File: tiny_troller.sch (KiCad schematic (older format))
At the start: 30 parts, among them U1 MA702GQ-P, U3 STM32G071G8U6, U5 MCP2025-330E_MD, U6 MAX14870ETC+T

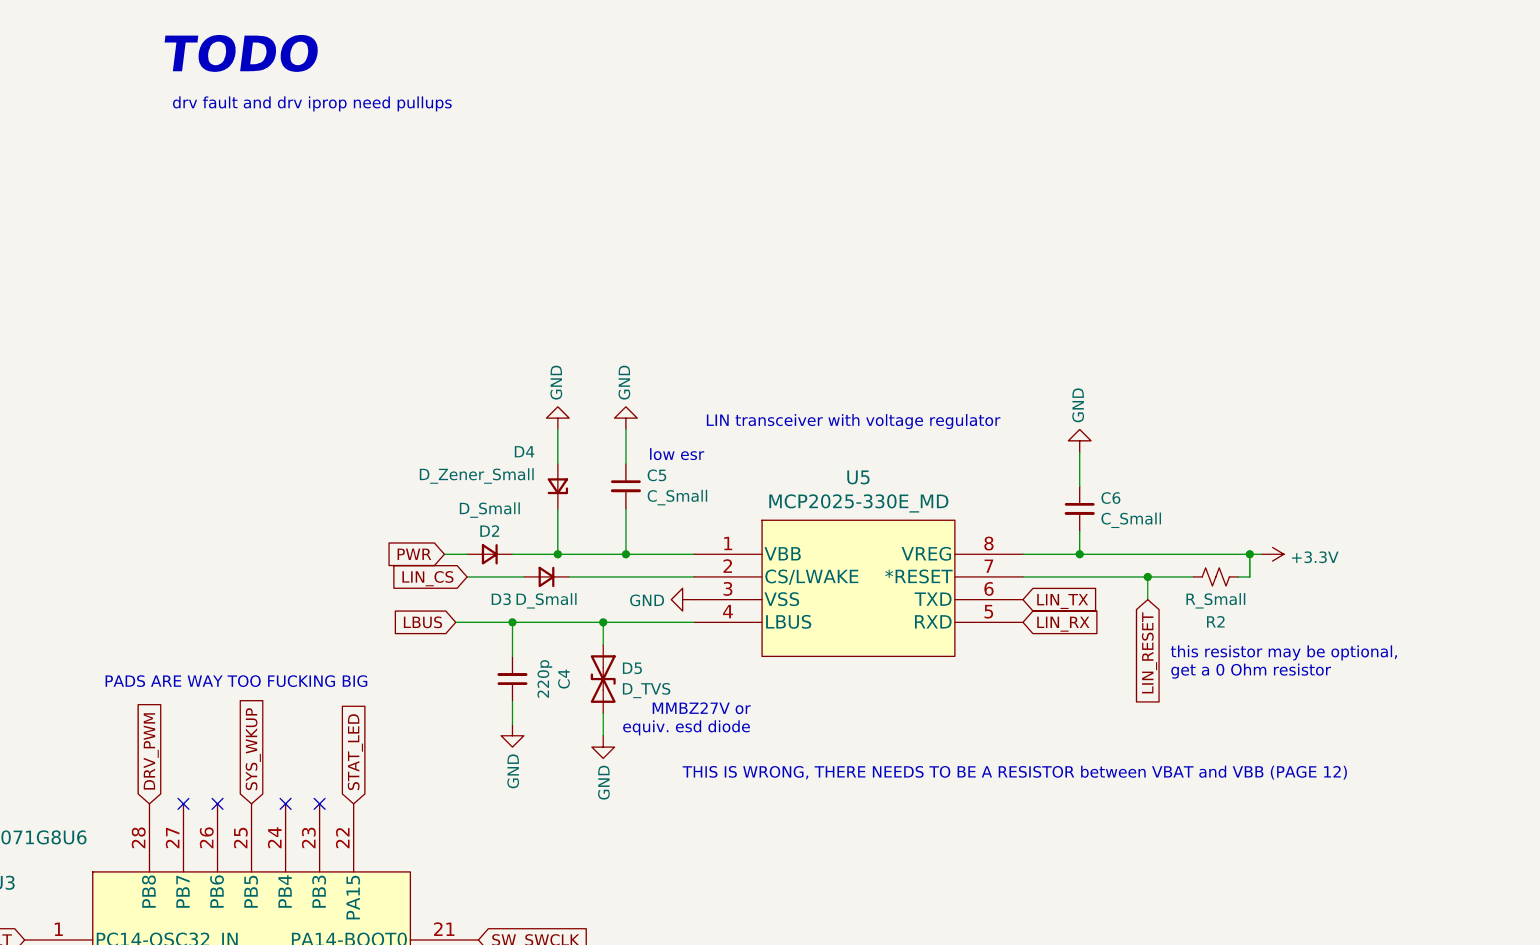
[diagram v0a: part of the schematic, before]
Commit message: R5 added, circuitry for MCP2025 LIN transceiver and regulator VBB pin should be correct now.
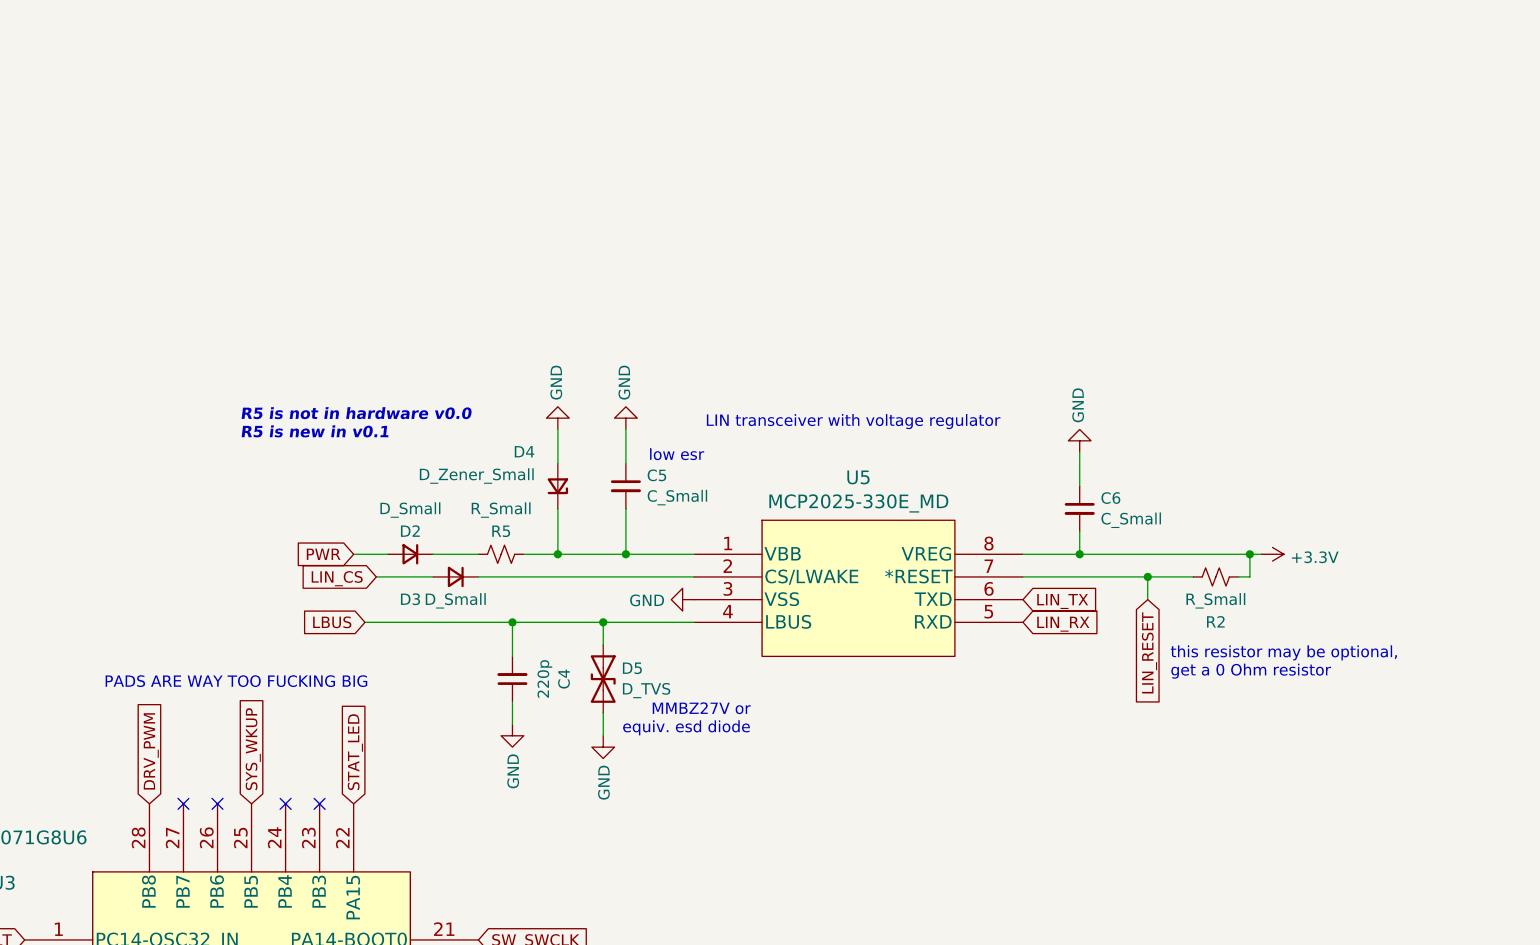
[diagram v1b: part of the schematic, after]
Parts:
- added R5: R_Small, Resistor_SMD:R_0402_1005Metric, symbol Device:R_Small_US
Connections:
- net at C5.2, D4.1 (K), U5.1 (VBB): now also R5.1; no longer D2.1 (K)
- new net: D2.1 (K), R5.2
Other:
- note added: "R5 is not in hardware v0.0\nR5 is new in v0.1"
- note removed: "THIS IS WRONG, THERE NEEDS TO BE A RESISTOR between VBAT and VBB (PAGE 12)"
- note removed: "TODO"
- note removed: "drv fault and drv iprop need pullups"
- moved on the sheet: D2, D3
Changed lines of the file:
@@
 Text GLabel 2800 7300 2    50   Input ~ 0
 STAT_LED
-Text Notes 5950 -550 0    157  Italic 31
-TODO
 Text GLabel 1850 1850 0    50   Input ~ 0
 LBUS
@@
 	0    1    1    0
 $EndComp
-Text Notes 6000 -400 0    50   ~ 0
-drv fault and drv iprop need pullups
 Text GLabel 7350 4000 2    50   Input ~ 0
 ENC_MGH
@@
 Wire Wire Line
 	10000 1250 10000 1100
-Text GLabel 7250 1850 0    50   Input ~ 0
+Text GLabel 6850 1850 0    50   Input ~ 0
 LBUS
 $Comp
@@
 L Device:D_Small D2
 U 1 1 615AA4A8
-P 7400 1550
-F 0 "D2" H 7400 1450 50  0000 C CNN
-F 1 "D_Small" H 7400 1350 50  0000 C CNN
-F 2 "Diode_SMD:D_0402_1005Metric" V 7400 1550 50  0001 C CNN
-F 3 "~" V 7400 1550 50  0001 C CNN
-	1    7400 1550
+P 7050 1550
+F 0 "D2" H 7050 1450 50  0000 C CNN
+F 1 "D_Small" H 7050 1350 50  0000 C CNN
+F 2 "Diode_SMD:D_0402_1005Metric" V 7050 1550 50  0001 C CNN
+F 3 "~" V 7050 1550 50  0001 C CNN
+	1    7050 1550
 	-1   0    0    1
 $EndComp
-Text GLabel 7200 1550 0    50   Input ~ 0
+Text GLabel 6800 1550 0    50   Input ~ 0
 PWR
 Wire Wire Line
@@
 Wire Wire Line
 	8000 1150 8000 1000
-Wire Wire Line
-	7500 1550 7700 1550
-Connection ~ 7700 1550
 $Comp
 L Device:C_Small C4
@@
 $EndComp
 Wire Wire Line
-	7250 1850 7500 1850
+	6850 1850 7500 1850
 Wire Wire Line
 	7500 1850 7500 2000
@@
 L Device:D_Small D3
 U 1 1 61617327
-P 7650 1650
-F 0 "D3" H 7850 1750 50  0000 C CNN
-F 1 "D_Small" H 7650 1750 50  0000 C CNN
-F 2 "Diode_SMD:D_0402_1005Metric" V 7650 1650 50  0001 C CNN
-F 3 "~" V 7650 1650 50  0001 C CNN
-	1    7650 1650
+P 7250 1650
+F 0 "D3" H 7450 1750 50  0000 C CNN
+F 1 "D_Small" H 7250 1750 50  0000 C CNN
+F 2 "Diode_SMD:D_0402_1005Metric" V 7250 1650 50  0001 C CNN
+F 3 "~" V 7250 1650 50  0001 C CNN
+	1    7250 1650
 	-1   0    0    1
 $EndComp
-Text GLabel 7300 1650 0    50   Input ~ 0
+Text GLabel 6900 1650 0    50   Input ~ 0
 LIN_CS
 Wire Wire Line
-	7300 1650 7550 1650
-Wire Wire Line
-	7750 1650 8300 1650
+	6900 1650 7150 1650
+Wire Wire Line
+	7350 1650 8300 1650
 $Comp
 L Device:C_Small C6
@@
 $EndComp
 Wire Wire Line
-	7200 1550 7300 1550
+	6800 1550 6950 1550
 Text Notes 5700 2150 0    50   ~ 0
 PADS ARE WAY TOO FUCKING BIG
@@
 	0    1    1    0
 $EndComp
-Text Notes 8250 2550 0    50   ~ 0
-THIS IS WRONG, THERE NEEDS TO BE A RESISTOR between VBAT and VBB (PAGE 12)
 Text Notes 10400 2100 0    50   ~ 0
 this resistor may be optional,\nget a 0 Ohm resistor
+$Comp
+L Device:R_Small_US R5
+U 1 1 618DD948
+P 7450 1550
+F 0 "R5" V 7350 1550 50  0000 C CNN
+F 1 "R_Small" V 7250 1550 50  0000 C CNN
+F 2 "Resistor_SMD:R_0402_1005Metric" H 7450 1550 50  0001 C CNN
+F 3 "~" H 7450 1550 50  0001 C CNN
+	1    7450 1550
+	0    1    1    0
+$EndComp
+Wire Wire Line
+	7550 1550 7700 1550
+Connection ~ 7700 1550
+Wire Wire Line
+	7350 1550 7150 1550
+Text Notes 6300 1050 0    50   Italic 10
+R5 is not in hardware v0.0\nR5 is new in v0.1
 $EndSCHEMATC

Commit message: v01 design first pass done (all components selected for the first time).
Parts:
- added C3: 100n, Capacitor_SMD:C_0402_1005Metric, symbol Device:C_Small
- C5: value C_Small -> 22u; V_max (none) -> 6.3V
- C6: value C_Small -> 10u; V_max (none) -> 6.3V
- D2, D3: value D_Small -> CLS10F40,L3F
- D4: value D_Zener_Small -> CPDQC24VEU-HF
- D5: value D_TVS -> CPDQR24V-HF
- R2: value R_Small -> 10k
- R3: value R_Small_US -> 70m
- R4: value R_Small_US -> 10k
- R5: value R_Small -> 2
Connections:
- net GND: now also C3.1
- net at D3.1 (K), U5.2 (CS/LWAKE): now also C3.2
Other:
- note added: "R2 and D3 may be optional,\ntry with 0 Ohm resistor instead"
- note removed: "MMBZ27V or\nequiv. esd diode"
- note removed: "PADS ARE WAY TOO FUCKING BIG"
- note removed: "low esr"
- note removed: "this resistor may be optional,\nget a 0 Ohm resistor"
- moved on the sheet: C4, C5, D3, D4, D5
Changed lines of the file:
@@
 Wire Wire Line
 	10000 1250 10000 1100
-Text GLabel 6850 1850 0    50   Input ~ 0
+Text GLabel 7600 1850 0    50   Input ~ 0
 LBUS
 $Comp
@@
 L Device:D_Zener_Small D4
 U 1 1 615A0B9A
-P 7700 1250
-F 0 "D4" V 7850 1150 50  0000 R CNN
-F 1 "D_Zener_Small" V 7750 1150 50  0000 R CNN
-F 2 "Diode_SMD:D_0402_1005Metric" V 7700 1250 50  0001 C CNN
-F 3 "~" V 7700 1250 50  0001 C CNN
-	1    7700 1250
+P 7700 1150
+F 0 "D4" V 7750 1050 50  0000 R CNN
+F 1 "CPDQC24VEU-HF" V 7650 1050 50  0000 R CNN
+F 2 "Diode_SMD:D_0402_1005Metric" V 7700 1150 50  0001 C CNN
+F 3 "~" V 7700 1150 50  0001 C CNN
+	1    7700 1150
 	0    1    -1   0
 $EndComp
@@
 U 1 1 615AA4A8
 P 7050 1550
-F 0 "D2" H 7050 1450 50  0000 C CNN
-F 1 "D_Small" H 7050 1350 50  0000 C CNN
+F 0 "D2" H 7050 1350 50  0000 C CNN
+F 1 "CLS10F40,L3F" H 7100 1450 50  0000 C CNN
 F 2 "Diode_SMD:D_0402_1005Metric" V 7050 1550 50  0001 C CNN
-F 3 "~" V 7050 1550 50  0001 C CNN
+F 3 "https://media.digikey.com/pdf/Data%20Sheets/Comchip%20PDFs/CPDQC24VEU-HF.pdf" V 7050 1550 50  0001 C CNN
 	1    7050 1550
 	-1   0    0    1
@@
 PWR
 Wire Wire Line
-	7700 1350 7700 1550
+	7700 1250 7700 1550
 Wire Wire Line
 	7700 1550 8000 1550
 Wire Wire Line
-	8000 1350 8000 1550
+	8000 1250 8000 1550
 Connection ~ 8000 1550
 Wire Wire Line
@@
 $EndComp
 Wire Wire Line
-	7700 1150 7700 1000
-Wire Wire Line
-	8000 1150 8000 1000
+	7700 1050 7700 1000
+Wire Wire Line
+	8000 1050 8000 1000
 $Comp
 L Device:C_Small C4
 U 1 1 615C8E0F
-P 7500 2100
-F 0 "C4" V 7271 2100 50  0000 C CNN
-F 1 "220p" V 7362 2100 50  0000 C CNN
-F 2 "Capacitor_SMD:C_0402_1005Metric" H 7500 2100 50  0001 C CNN
-F 3 "~" H 7500 2100 50  0001 C CNN
-	1    7500 2100
-	-1   0    0    1
-$EndComp
-Wire Wire Line
-	6850 1850 7500 1850
-Wire Wire Line
-	7500 1850 7500 2000
-Connection ~ 7500 1850
-Wire Wire Line
-	7500 1850 7900 1850
-Wire Wire Line
-	7900 1850 7900 1950
-Connection ~ 7900 1850
-Wire Wire Line
-	7900 1850 8300 1850
+P 7700 2100
+F 0 "C4" H 7850 2050 50  0000 C CNN
+F 1 "220p" H 7900 2150 50  0000 C CNN
+F 2 "Capacitor_SMD:C_0402_1005Metric" H 7700 2100 50  0001 C CNN
+F 3 "~" H 7700 2100 50  0001 C CNN
+	1    7700 2100
+	-1   0    0    1
+$EndComp
+Wire Wire Line
+	7700 1850 7700 2000
+Wire Wire Line
+	8000 1850 8000 1950
 $Comp
 L power:GND #PWR0108
 U 1 1 615DCA56
-P 7500 2300
-F 0 "#PWR0108" H 7500 2050 50  0001 C CNN
-F 1 "GND" V 7505 2172 50  0000 R CNN
-F 2 "" H 7500 2300 50  0001 C CNN
-F 3 "" H 7500 2300 50  0001 C CNN
-	1    7500 2300
+P 7700 2300
+F 0 "#PWR0108" H 7700 2050 50  0001 C CNN
+F 1 "GND" V 7705 2172 50  0000 R CNN
+F 2 "" H 7700 2300 50  0001 C CNN
+F 3 "" H 7700 2300 50  0001 C CNN
+	1    7700 2300
 	1    0    0    -1
 $EndComp
@@
 L power:GND #PWR0109
 U 1 1 615DD075
-P 7900 2350
-F 0 "#PWR0109" H 7900 2100 50  0001 C CNN
-F 1 "GND" V 7905 2222 50  0000 R CNN
-F 2 "" H 7900 2350 50  0001 C CNN
-F 3 "" H 7900 2350 50  0001 C CNN
-	1    7900 2350
-	1    0    0    -1
-$EndComp
-Wire Wire Line
-	7500 2200 7500 2300
-Wire Wire Line
-	7900 2250 7900 2350
-Text Notes 8550 2350 2    50   ~ 0
-MMBZ27V or\nequiv. esd diode
-Text Notes 8100 1150 0    50   ~ 0
-low esr
+P 8000 2350
+F 0 "#PWR0109" H 8000 2100 50  0001 C CNN
+F 1 "GND" V 8005 2222 50  0000 R CNN
+F 2 "" H 8000 2350 50  0001 C CNN
+F 3 "" H 8000 2350 50  0001 C CNN
+	1    8000 2350
+	1    0    0    -1
+$EndComp
+Wire Wire Line
+	7700 2200 7700 2300
+Wire Wire Line
+	8000 2250 8000 2350
 $Comp
 L Device:R_Small_US R2
@@
 P 10600 1650
 F 0 "R2" V 10400 1650 50  0000 C CNN
-F 1 "R_Small" V 10500 1650 50  0000 C CNN
+F 1 "10k" V 10500 1650 50  0000 C CNN
 F 2 "Resistor_SMD:R_0402_1005Metric" H 10600 1650 50  0001 C CNN
 F 3 "~" H 10600 1650 50  0001 C CNN
@@
 $EndComp
 Wire Wire Line
-	9750 1650 10300 1650
-Text GLabel 10300 1750 3    50   Input ~ 0
+	9750 1650 10250 1650
+Text GLabel 10250 1750 3    50   Input ~ 0
 LIN_RESET
 Wire Wire Line
-	10300 1750 10300 1650
-Connection ~ 10300 1650
-Wire Wire Line
-	10300 1650 10500 1650
+	10250 1750 10250 1650
 Connection ~ 10000 1550
 Wire Wire Line
@@
 L Device:D_Small D3
 U 1 1 61617327
-P 7250 1650
-F 0 "D3" H 7450 1750 50  0000 C CNN
-F 1 "D_Small" H 7250 1750 50  0000 C CNN
-F 2 "Diode_SMD:D_0402_1005Metric" V 7250 1650 50  0001 C CNN
-F 3 "~" V 7250 1650 50  0001 C CNN
-	1    7250 1650
-	-1   0    0    1
-$EndComp
-Text GLabel 6900 1650 0    50   Input ~ 0
+P 6800 1650
+F 0 "D3" H 6800 1750 50  0000 C CNN
+F 1 "CLS10F40,L3F" H 6800 1850 50  0000 C CNN
+F 2 "Diode_SMD:D_0402_1005Metric" V 6800 1650 50  0001 C CNN
+F 3 "~" V 6800 1650 50  0001 C CNN
+	1    6800 1650
+	-1   0    0    1
+$EndComp
+Text GLabel 6550 1650 0    50   Input ~ 0
 LIN_CS
 Wire Wire Line
-	6900 1650 7150 1650
-Wire Wire Line
-	7350 1650 8300 1650
+	6550 1650 6700 1650
+Wire Wire Line
+	6900 1650 7100 1650
 $Comp
 L Device:C_Small C6
 U 1 1 61637AA0
 P 10000 1350
-F 0 "C6" H 10092 1396 50  0000 L CNN
-F 1 "C_Small" H 10092 1305 50  0000 L CNN
+F 0 "C6" H 10100 1450 50  0000 L CNN
+F 1 "10u" H 10100 1350 50  0000 L CNN
 F 2 "Capacitor_SMD:C_0402_1005Metric" H 10000 1350 50  0001 C CNN
-F 3 "~" H 10000 1350 50  0001 C CNN
+F 3 "GRJ155R60J106ME11D" H 10000 1350 50  0001 C CNN
+F 4 "6.3V" H 10100 1300 50  0000 L TNN "V_max"
 	1    10000 1350
 	1    0    0    -1
@@
 L Device:C_Small C5
 U 1 1 61638882
-P 8000 1250
-F 0 "C5" H 8092 1296 50  0000 L CNN
-F 1 "C_Small" H 8092 1205 50  0000 L CNN
-F 2 "Capacitor_SMD:C_0402_1005Metric" H 8000 1250 50  0001 C CNN
-F 3 "~" H 8000 1250 50  0001 C CNN
-	1    8000 1250
+P 8000 1150
+F 0 "C5" H 8092 1196 50  0000 L CNN
+F 1 "22u" H 8092 1105 50  0000 L CNN
+F 2 "Capacitor_SMD:C_0402_1005Metric" H 8000 1150 50  0001 C CNN
+F 3 "04026D226MAT2A" H 8000 1150 50  0001 C CNN
+F 4 "6.3V" H 8100 1050 50  0000 L TNN "V_max"
+	1    8000 1150
 	1    0    0    -1
 $EndComp
 Wire Wire Line
 	6800 1550 6950 1550
-Text Notes 5700 2150 0    50   ~ 0
-PADS ARE WAY TOO FUCKING BIG
 $Comp
 L power:GND #PWR0110
@@
 P 6850 5800
 F 0 "R3" V 6650 5800 50  0000 C CNN
-F 1 "R_Small_US" V 6750 5800 50  0000 C CNN
+F 1 "70m" V 6750 5800 50  0000 C CNN
 F 2 "Resistor_SMD:R_0402_1005Metric" H 6850 5800 50  0001 C CNN
-F 3 "~" H 6850 5800 50  0001 C CNN
+F 3 "ERJ-2BWFR082X" H 6850 5800 50  0001 C CNN
 	1    6850 5800
 	1    0    0    -1
@@
 P 10000 6050
 F 0 "R4" V 9800 6050 50  0000 C CNN
-F 1 "R_Small_US" V 9900 6050 50  0000 C CNN
+F 1 "10k" V 9900 6050 50  0000 C CNN
 F 2 "Resistor_SMD:R_0402_1005Metric" H 10000 6050 50  0001 C CNN
 F 3 "~" H 10000 6050 50  0001 C CNN
@@
 L Device:D_TVS D5
 U 1 1 61851569
-P 7900 2100
-F 0 "D5" V 7854 2180 50  0000 L CNN
-F 1 "D_TVS" V 7945 2180 50  0000 L CNN
-F 2 "Diode_SMD:D_0402_1005Metric" H 7900 2100 50  0001 C CNN
-F 3 "~" H 7900 2100 50  0001 C CNN
-	1    7900 2100
+P 8000 2100
+F 0 "D5" V 7954 2180 50  0000 L CNN
+F 1 "CPDQR24V-HF" V 8045 2180 50  0000 L CNN
+F 2 "Diode_SMD:D_0402_1005Metric" H 8000 2100 50  0001 C CNN
+F 3 "https://www.mouser.com/datasheet/2/80/CPDQR24V_HF_RevB389741-2505549.pdf" H 8000 2100 50  0001 C CNN
+	1    8000 2100
 	0    1    1    0
 $EndComp
-Text Notes 10400 2100 0    50   ~ 0
-this resistor may be optional,\nget a 0 Ohm resistor
 $Comp
 L Device:R_Small_US R5
@@
 P 7450 1550
 F 0 "R5" V 7350 1550 50  0000 C CNN
-F 1 "R_Small" V 7250 1550 50  0000 C CNN
+F 1 "2" V 7250 1550 50  0000 C CNN
 F 2 "Resistor_SMD:R_0402_1005Metric" H 7450 1550 50  0001 C CNN
-F 3 "~" H 7450 1550 50  0001 C CNN
+F 3 "CRCW04022R00JNED" H 7450 1550 50  0001 C CNN
 	1    7450 1550
 	0    1    1    0
@@
 Text Notes 6300 1050 0    50   Italic 10
 R5 is not in hardware v0.0\nR5 is new in v0.1
+Connection ~ 8000 1850
+Wire Wire Line
+	8000 1850 8300 1850
+Connection ~ 7700 1850
+Wire Wire Line
+	7700 1850 8000 1850
+Wire Wire Line
+	7600 1850 7700 1850
+Connection ~ 10250 1650
+Wire Wire Line
+	10250 1650 10500 1650
+Text Notes 8500 2500 0    50   ~ 0
+R2 and D3 may be optional,\ntry with 0 Ohm resistor instead
+$Comp
+L Device:C_Small C3
+U 1 1 6198FA51
+P 7100 2050
+F 0 "C3" H 7250 2000 50  0000 C CNN
+F 1 "100n" H 7300 2100 50  0000 C CNN
+F 2 "Capacitor_SMD:C_0402_1005Metric" H 7100 2050 50  0001 C CNN
+F 3 "~" H 7100 2050 50  0001 C CNN
+	1    7100 2050
+	-1   0    0    1
+$EndComp
+Wire Wire Line
+	7100 1650 7100 1950
+Connection ~ 7100 1650
+Wire Wire Line
+	7100 1650 8300 1650
+$Comp
+L power:GND #PWR0116
+U 1 1 61991DBF
+P 7100 2200
+F 0 "#PWR0116" H 7100 1950 50  0001 C CNN
+F 1 "GND" V 7105 2072 50  0000 R CNN
+F 2 "" H 7100 2200 50  0001 C CNN
+F 3 "" H 7100 2200 50  0001 C CNN
+	1    7100 2200
+	1    0    0    -1
+$EndComp
+Wire Wire Line
+	7100 2150 7100 2200
 $EndSCHEMATC
